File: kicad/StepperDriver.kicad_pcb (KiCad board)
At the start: 2 copper layers, 71 x 70 mm, 120 parts, among them J1 Phase 1, J10 2A, J11 3A, J12 3A, J13 4A, J14 4A, J15 5A, J16 5A, J2 BOOT0, J3 Phase 2, J4 Power In, J5 USART, J6 Control IO, J7 1A, J8 1A, J9 2A, SW1 Reset, U1 AP7370, U10 FAN3278, U11 FAN3278, U12 MCP6L02, U13 FAN3278, U14 FAN3278, U15 STM32F303K6Tx, U2 FDS4435BZ, U3 FDS4435BZ, U4 FDS4435BZ, U5 FDS4435BZ, U6 DMG4496SSS, U7 DMG4496SSS, U8 DMG4496SSS, U9 DMG4496SSS

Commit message: Minor change
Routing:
- net GND: track 63.8 -> 51.1 mm
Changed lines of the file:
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@@
     (thickness 1.6)
     (drawings 25)
-    (tracks 637)
+    (tracks 630)
     (zones 0)
     (modules 120)
@@
   (segment (start 64.975 44) (end 63.7 44) (width 0.25) (layer F.Cu) (net 1))
   (segment (start 63.7 44) (end 63.1 44.6) (width 0.25) (layer F.Cu) (net 1))
-  (segment (start 64.975 55) (end 64.975 53) (width 0.25) (layer F.Cu) (net 1))
   (via (at 62.7 59.5) (size 0.7) (drill 0.4) (layers F.Cu B.Cu) (net 1))
   (segment (start 64.975 59.5) (end 62.7 59.5) (width 0.25) (layer F.Cu) (net 1))
@@
   (segment (start 6 53.975) (end 6.025 54) (width 0.25) (layer F.Cu) (net 1))
   (via (at 63.1 44.6) (size 0.7) (drill 0.4) (layers F.Cu B.Cu) (net 1))
-  (segment (start 64.975 48.5) (end 66 49.525) (width 0.25) (layer F.Cu) (net 1))
-  (segment (start 66 51.975) (end 64.975 53) (width 0.25) (layer F.Cu) (net 1))
-  (segment (start 66 49.525) (end 66 51.975) (width 0.25) (layer F.Cu) (net 1))
-  (segment (start 64.975 55) (end 66 56.025) (width 0.25) (layer F.Cu) (net 1))
-  (segment (start 66 58.475) (end 64.975 59.5) (width 0.25) (layer F.Cu) (net 1))
-  (segment (start 66 56.025) (end 66 58.475) (width 0.25) (layer F.Cu) (net 1))
   (via (at 54.5 15.7) (size 0.7) (drill 0.4) (layers F.Cu B.Cu) (net 1))
   (via (at 21.1 15.8) (size 0.7) (drill 0.4) (layers F.Cu B.Cu) (net 1))

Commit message: Added Dwgs.User layer
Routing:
- net GND: vias 51 -> 52
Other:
- board size 71 x 70 mm -> 71 x 70.5 mm
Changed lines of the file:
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@@
   (general
     (thickness 1.6)
-    (drawings 25)
-    (tracks 630)
+    (drawings 26)
+    (tracks 631)
     (zones 0)
     (modules 120)
@@
   (page A4)
   (layers
-    (0 F.Cu signal)
-    (31 B.Cu signal)
+    (0 F.Cu mixed)
+    (31 B.Cu mixed)
     (36 B.SilkS user)
     (37 F.SilkS user)
     (38 B.Mask user)
     (39 F.Mask user)
+    (40 Dwgs.User user)
     (44 Edge.Cuts user)
     (45 Margin user)
@@
     )
   )
+  (gr_line (start 0 -0.5) (end 71 -0.5) (layer Edge.Cuts) (width 0.05))
   (gr_text GND (at 5.5 68) (layer F.SilkS)
     (effects (font (size 2 2) (thickness 0.3)))
@@
   (via (at 17.8 3.2) (size 0.7) (drill 0.4) (layers F.Cu B.Cu) (net 1))
   (via (at 2.3 3.5) (size 0.7) (drill 0.4) (layers F.Cu B.Cu) (net 1))
+  (via (at 24.4 48.6) (size 0.7) (drill 0.4) (layers F.Cu B.Cu) (net 1))
   (via (at 61.5 30.5) (size 0.7) (drill 0.4) (layers F.Cu B.Cu) (net 2))
   (via (at 63 30.5) (size 0.7) (drill 0.4) (layers F.Cu B.Cu) (net 2))

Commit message: Added layer outline to Dwgs.User layer for easier panelization
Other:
- board size 71 x 70.5 mm -> 71 x 70 mm
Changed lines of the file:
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@@
   (general
     (thickness 1.6)
-    (drawings 26)
+    (drawings 29)
     (tracks 631)
     (zones 0)
@@
     )
   )
-  (gr_line (start 0 -0.5) (end 71 -0.5) (layer Edge.Cuts) (width 0.05))
+  (gr_line (start 0 0) (end 0 70) (layer Dwgs.User) (width 0.05))
+  (gr_line (start 71 70) (end 0 70) (layer Dwgs.User) (width 0.05))
+  (gr_line (start 71 0) (end 71 70) (layer Dwgs.User) (width 0.05))
+  (gr_line (start 0 0) (end 71 0) (layer Dwgs.User) (width 0.05))
   (gr_text GND (at 5.5 68) (layer F.SilkS)
     (effects (font (size 2 2) (thickness 0.3)))

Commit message: Added silkscreen stuff
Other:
- board text added: "1"
- board text added: "2"
- board text added: "Phase 1"
- board text added: "Phase 2"
- board text added: "REV1"
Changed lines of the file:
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@@
   (general
     (thickness 1.6)
-    (drawings 29)
+    (drawings 36)
     (tracks 631)
     (zones 0)
@@
     )
   )
+  (gr_text 1 (at 51 1) (layer F.SilkS)
+    (effects (font (size 1 1) (thickness 0.15)))
+  )
+  (gr_text 2 (at 54.5 1) (layer F.SilkS)
+    (effects (font (size 1 1) (thickness 0.15)))
+  )
+  (gr_text 2 (at 19.5 1) (layer F.SilkS)
+    (effects (font (size 1 1) (thickness 0.15)))
+  )
+  (gr_text 1 (at 16 1) (layer F.SilkS)
+    (effects (font (size 1 1) (thickness 0.15)))
+  )
+  (gr_text "Phase 2" (at 42.5 35) (layer F.SilkS)
+    (effects (font (size 1 1) (thickness 0.15)))
+  )
+  (gr_text "Phase 1" (at 28.5 35) (layer F.SilkS)
+    (effects (font (size 1 1) (thickness 0.15)))
+  )
+  (gr_text REV1 (at 58.5 69) (layer F.SilkS)
+    (effects (font (size 1 1) (thickness 0.15)))
+  )
   (gr_line (start 0 0) (end 0 70) (layer Dwgs.User) (width 0.05))

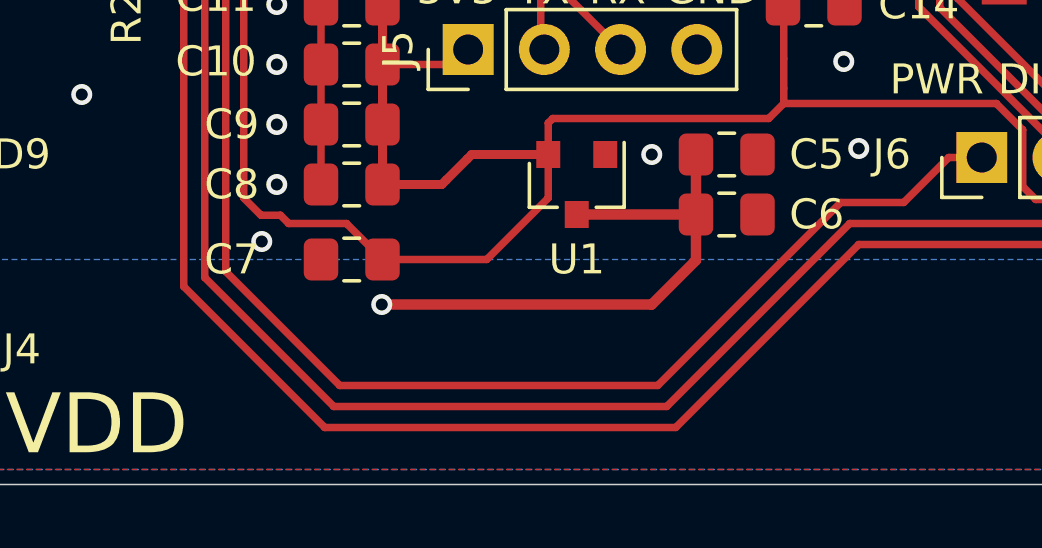
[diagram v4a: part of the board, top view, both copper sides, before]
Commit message: Moved some traces
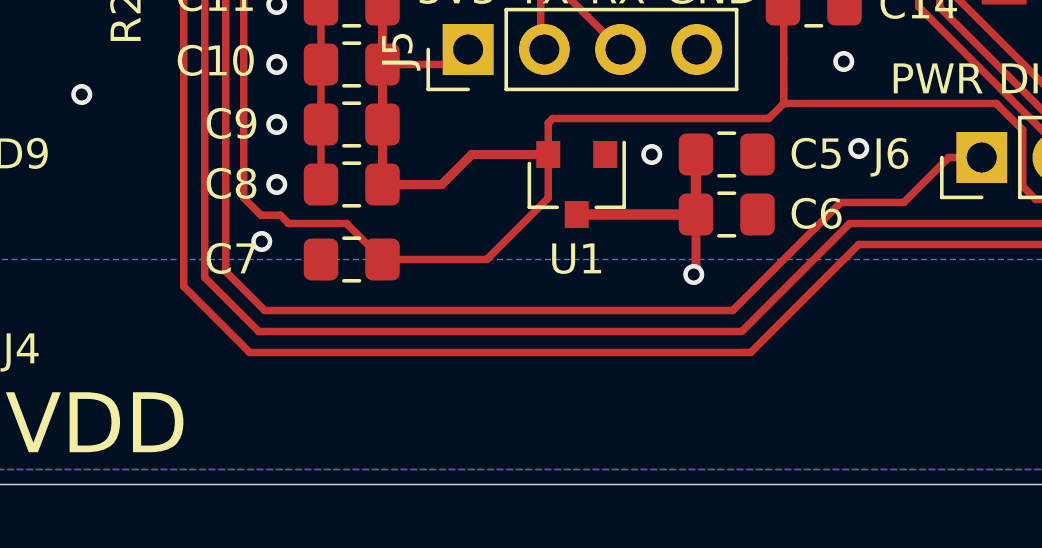
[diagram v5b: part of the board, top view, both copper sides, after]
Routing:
- net VDD: track 121.8 -> 111.2 mm
- net /P2_SENSE: track 99.1 -> 97.0 mm
- net /IN_PWR: track 50.2 -> 48.1 mm
- net /CurrentSelection/P2_GAIN: track 81.3 -> 79.2 mm
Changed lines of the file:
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@@
     (thickness 1.6)
     (drawings 36)
-    (tracks 631)
+    (tracks 630)
     (zones 0)
     (modules 120)
@@
   (segment (start 39.475 59) (end 39.475 61) (width 0.35) (layer F.Cu) (net 2))
   (segment (start 39.475 61) (end 35.5 61) (width 0.35) (layer F.Cu) (net 2))
-  (segment (start 39.475 61) (end 39.475 62.525) (width 0.35) (layer F.Cu) (net 2))
-  (via (at 29 64) (size 0.7) (drill 0.4) (layers F.Cu B.Cu) (net 2))
-  (segment (start 39.475 62.525) (end 38 64) (width 0.35) (layer F.Cu) (net 2))
-  (segment (start 38 64) (end 29 64) (width 0.35) (layer F.Cu) (net 2))
+  (via (at 39.4 63) (size 0.7) (drill 0.4) (layers F.Cu B.Cu) (net 2))
+  (segment (start 39.475 61) (end 39.475 62.925) (width 0.3) (layer F.Cu) (net 2))
+  (segment (start 39.475 62.925) (end 39.4 63) (width 0.3) (layer F.Cu) (net 2))
   (segment (start 34.55 59) (end 32 59) (width 0.3) (layer F.Cu) (net 3))
   (segment (start 42.4 56.8) (end 42.4 57.3) (width 0.25) (layer F.Cu) (net 3))
@@
   (segment (start 34.3 55.38) (end 34.42 55.5) (width 0.25) (layer F.Cu) (net 13))
   (segment (start 34.3 50.675) (end 34.3 55.38) (width 0.25) (layer F.Cu) (net 13))
-  (segment (start 27.6 66.7) (end 23.8 62.9) (width 0.25) (layer F.Cu) (net 14))
-  (segment (start 38.2 66.7) (end 27.6 66.7) (width 0.25) (layer F.Cu) (net 14))
-  (segment (start 46.4 60.6) (end 44.3 60.6) (width 0.25) (layer F.Cu) (net 14))
-  (segment (start 47.9 59.1) (end 46.4 60.6) (width 0.25) (layer F.Cu) (net 14))
-  (segment (start 49 59.1) (end 47.9 59.1) (width 0.25) (layer F.Cu) (net 14))
   (via (at 26.822702 48.397702) (size 0.7) (drill 0.4) (layers F.Cu B.Cu) (net 14))
-  (segment (start 23.8 51.420404) (end 26.822702 48.397702) (width 0.25) (layer F.Cu) (net 14))
   (segment (start 28.397702 48.397702) (end 28.5 48.5) (width 0.25) (layer B.Cu) (net 14))
   (via (at 28.5 48.5) (size 0.7) (drill 0.4) (layers F.Cu B.Cu) (net 14))
   (segment (start 28.5 48.5) (end 31.325 48.5) (width 0.25) (layer F.Cu) (net 14))
   (segment (start 26.822702 48.397702) (end 28.397702 48.397702) (width 0.25) (layer B.Cu) (net 14))
-  (segment (start 44.3 60.6) (end 38.2 66.7) (width 0.25) (layer F.Cu) (net 14))
+  (segment (start 23.8 51.420404) (end 26.822702 48.397702) (width 0.25) (layer F.Cu) (net 14))
   (segment (start 23.8 62.9) (end 23.8 51.420404) (width 0.25) (layer F.Cu) (net 14))
+  (segment (start 47.9 59.1) (end 46.4 60.6) (width 0.25) (layer F.Cu) (net 14))
+  (segment (start 49 59.1) (end 47.9 59.1) (width 0.25) (layer F.Cu) (net 14))
+  (segment (start 46.4 60.6) (end 44.3 60.6) (width 0.25) (layer F.Cu) (net 14))
+  (segment (start 44.3 60.6) (end 40.7 64.2) (width 0.25) (layer F.Cu) (net 14))
+  (segment (start 40.7 64.2) (end 25.1 64.2) (width 0.25) (layer F.Cu) (net 14))
+  (segment (start 25.1 64.2) (end 23.8 62.9) (width 0.25) (layer F.Cu) (net 14))
   (segment (start 41.3 50) (end 41.3 46.875) (width 0.25) (layer F.Cu) (net 15))
   (segment (start 46.9 54.078587) (end 46.9 51.9) (width 0.25) (layer F.Cu) (net 15))
@@
   (segment (start 21.8 50) (end 21.8 51.3) (width 0.25) (layer F.Cu) (net 19))
   (segment (start 21.8 51.3) (end 21.575 51.525) (width 0.25) (layer F.Cu) (net 19))
-  (segment (start 58.85 56.65) (end 58.85 54) (width 0.25) (layer F.Cu) (net 19))
   (segment (start 59.7 57.5) (end 58.85 56.65) (width 0.25) (layer F.Cu) (net 19))
   (segment (start 59.7 61.1) (end 59.7 57.5) (width 0.25) (layer F.Cu) (net 19))
+  (segment (start 58.8 62) (end 59.7 61.1) (width 0.25) (layer F.Cu) (net 19))
   (segment (start 44.9 62) (end 58.8 62) (width 0.25) (layer F.Cu) (net 19))
   (segment (start 21.725 51.525) (end 22.4 52.2) (width 0.25) (layer F.Cu) (net 19))
   (segment (start 21.575 51.525) (end 21.725 51.525) (width 0.25) (layer F.Cu) (net 19))
+  (segment (start 58.85 56.65) (end 58.85 54) (width 0.25) (layer F.Cu) (net 19))
+  (segment (start 22.4 63.4) (end 24.6 65.6) (width 0.25) (layer F.Cu) (net 19))
+  (segment (start 24.6 65.6) (end 41.3 65.6) (width 0.25) (layer F.Cu) (net 19))
   (segment (start 22.4 52.2) (end 22.4 63.4) (width 0.25) (layer F.Cu) (net 19))
-  (segment (start 58.8 62) (end 59.7 61.1) (width 0.25) (layer F.Cu) (net 19))
-  (segment (start 22.4 63.4) (end 27.1 68.1) (width 0.25) (layer F.Cu) (net 19))
-  (segment (start 27.1 68.1) (end 38.8 68.1) (width 0.25) (layer F.Cu) (net 19))
-  (segment (start 38.8 68.1) (end 44.9 62) (width 0.25) (layer F.Cu) (net 19))
+  (segment (start 41.3 65.6) (end 44.9 62) (width 0.25) (layer F.Cu) (net 19))
   (segment (start 70.075 39.475) (end 69 39.475) (width 0.25) (layer F.Cu) (net 20))
   (segment (start 60.15 44) (end 61.2 44) (width 0.25) (layer F.Cu) (net 20))
@@
   (segment (start 56.5 55.3) (end 56.5 40.7) (width 0.25) (layer F.Cu) (net 30))
   (segment (start 59 57.8) (end 56.5 55.3) (width 0.25) (layer F.Cu) (net 30))
-  (segment (start 59 60.8) (end 59 57.8) (width 0.25) (layer F.Cu) (net 30))
-  (segment (start 58.5 61.3) (end 59 60.8) (width 0.25) (layer F.Cu) (net 30))
+  (segment (start 56.5 40.7) (end 55.4 39.6) (width 0.25) (layer F.Cu) (net 30))
   (segment (start 44.6 61.3) (end 58.5 61.3) (width 0.25) (layer F.Cu) (net 30))
   (segment (start 25.975 48.325) (end 23.1 51.2) (width 0.25) (layer F.Cu) (net 30))
+  (segment (start 58.5 61.3) (end 59 60.8) (width 0.25) (layer F.Cu) (net 30))
   (segment (start 25.975 47.405) (end 25.975 48.325) (width 0.25) (layer F.Cu) (net 30))
   (segment (start 23.1 51.2) (end 23.1 63.1) (width 0.25) (layer F.Cu) (net 30))
-  (segment (start 56.5 40.7) (end 55.4 39.6) (width 0.25) (layer F.Cu) (net 30))
-  (segment (start 23.1 63.1) (end 27.4 67.4) (width 0.25) (layer F.Cu) (net 30))
-  (segment (start 27.4 67.4) (end 38.5 67.4) (width 0.25) (layer F.Cu) (net 30))
-  (segment (start 38.5 67.4) (end 44.6 61.3) (width 0.25) (layer F.Cu) (net 30))
+  (segment (start 23.1 63.1) (end 24.9 64.9) (width 0.25) (layer F.Cu) (net 30))
+  (segment (start 24.9 64.9) (end 41 64.9) (width 0.25) (layer F.Cu) (net 30))
+  (segment (start 59 60.8) (end 59 57.8) (width 0.25) (layer F.Cu) (net 30))
+  (segment (start 41 64.9) (end 44.6 61.3) (width 0.25) (layer F.Cu) (net 30))
   (segment (start 48.25 42.25) (end 49.75 42.25) (width 0.25) (layer F.Cu) (net 31))
   (segment (start 44.025 40.5) (end 46.5 40.5) (width 0.25) (layer F.Cu) (net 31))
